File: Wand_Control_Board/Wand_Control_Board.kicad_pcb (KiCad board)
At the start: 2 copper layers, 11.5 x 40.1 mm, 6 parts, among them J1 Conn_01x03_Socket, J2 Conn_01x03_Socket, J3 Conn_01x03_Socket, J5 Conn_01x05_Socket, J8 Conn_01x02_Socket, U1 ATtiny85-20P

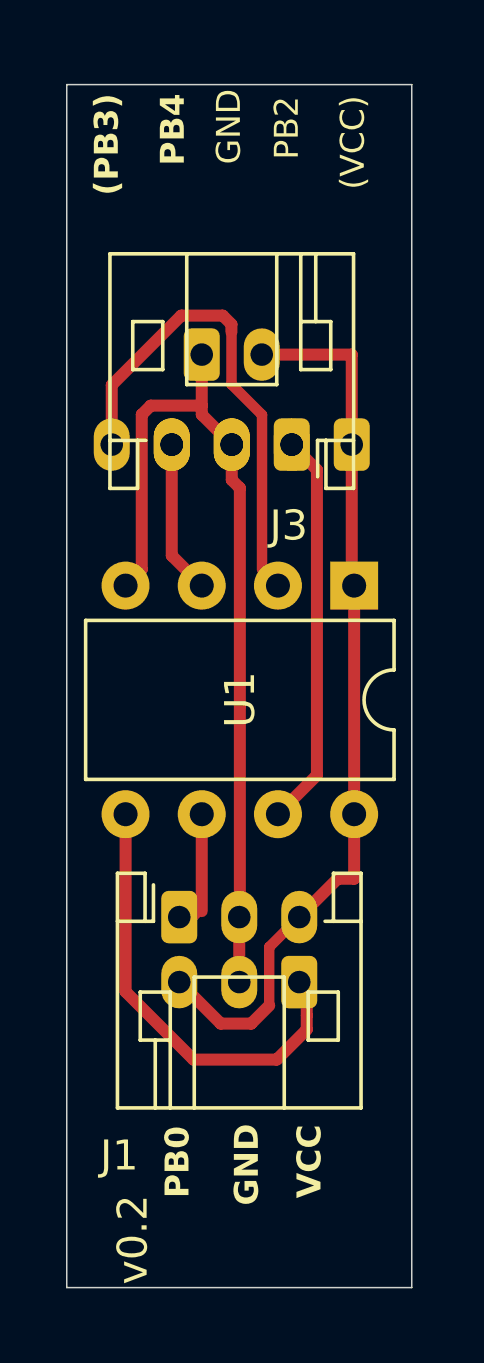
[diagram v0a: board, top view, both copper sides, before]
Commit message: added unneeded prog pad
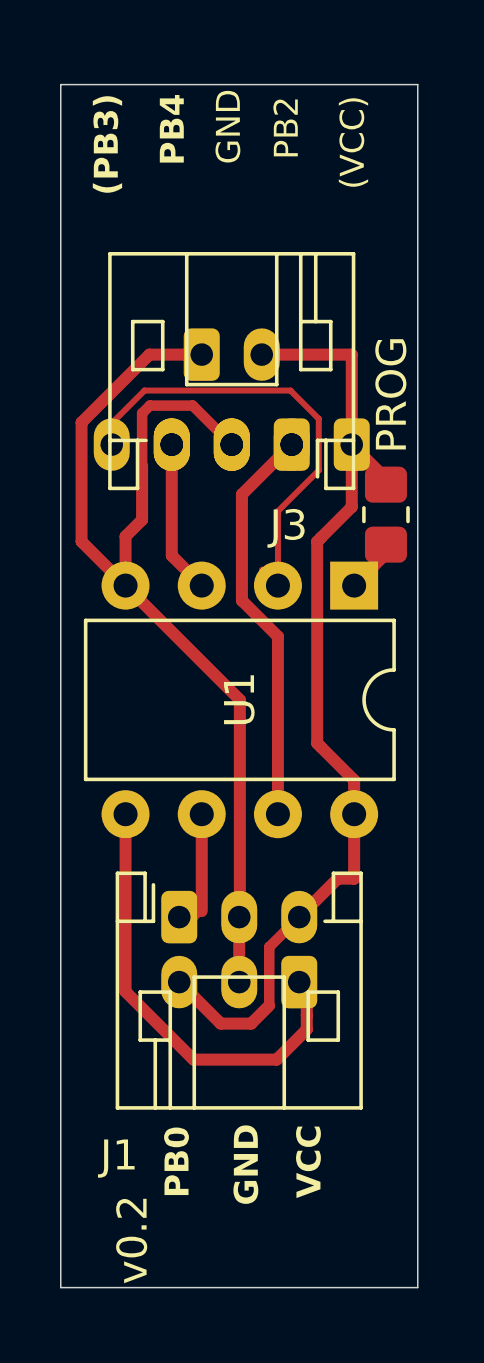
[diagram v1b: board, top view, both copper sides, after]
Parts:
- added PROG: 0, Resistor_SMD:R_0805_2012Metric_Pad1.20x1.40mm_HandSolder, F.Cu at (155.6, 54.8)
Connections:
- J5 pad 2: Net-(J3-Pin_1) -> Net-(J3-Pin_3)
- J5 pad 4: Net-(J3-Pin_3) -> Net-(J3-Pin_1)
- U1 pad 1: VCC -> Net-(U1-~{RESET}/PB5)
- U1 pad 3: Net-(J3-Pin_1) -> Net-(J3-Pin_3)
- U1 pad 7: Net-(J3-Pin_3) -> Net-(J3-Pin_1)
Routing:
- net Net-(J3-Pin_1): track 5.11 -> 13.5 mm
- net Net-(J3-Pin_3): track 13.2 -> 5.11 mm
- net GND: track 29.9 -> 35.8 mm
- net VCC: track 30.0 -> 33.0 mm
- net Net-(J5-Pin_5): track 16.4 -> 14.6 mm
- net Net-(U1-~{RESET}/PB5): track 0.00 -> 1.74 mm
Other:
- board size 11.5 x 40.1 mm -> 11.9 x 40.1 mm

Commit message: removed unneeded progam pad
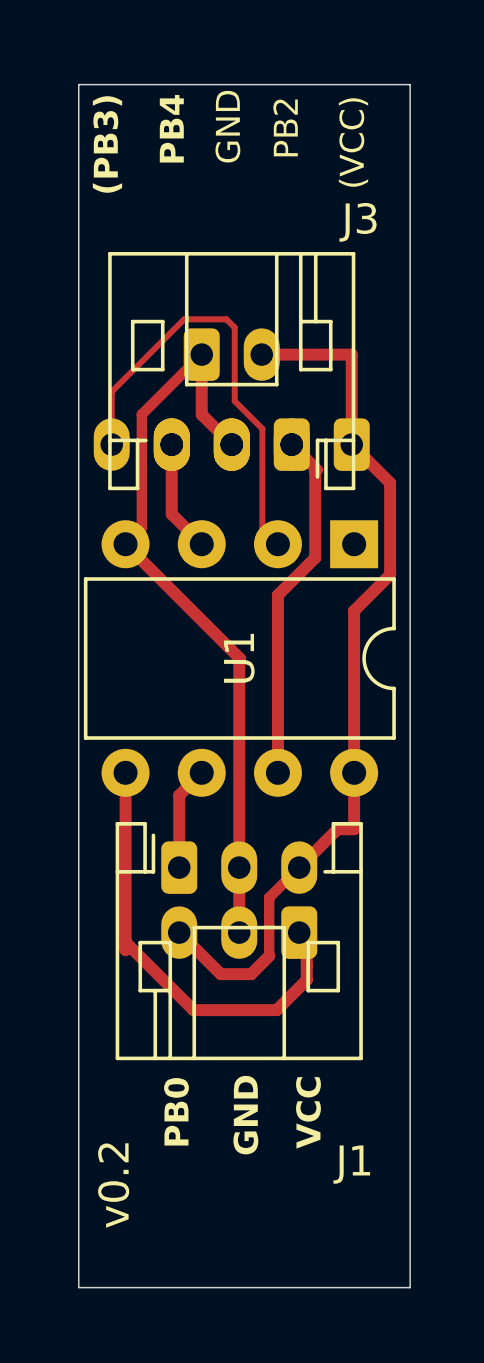
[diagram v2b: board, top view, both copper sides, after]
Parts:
- removed PROG: 0, Resistor_SMD:R_0805_2012Metric_Pad1.20x1.40mm_HandSolder
- moved J1 1.65 mm to (148.8, 66.6)
- moved J2 1.65 mm to (152.8, 68.8)
- moved U1 1.38 mm to (154.6, 55.8)
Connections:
- J5 pad 4: Net-(J3-Pin_1) -> Net-(J3-Pin_3)
- U1 pad 1: Net-(U1-~{RESET}/PB5) -> unconnected-(U1-~{RESET}/PB5-Pad1)
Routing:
- net GND: track 35.8 -> 26.3 mm
- net VCC: track 33.0 -> 29.4 mm
- net Net-(J3-Pin_1): track 13.5 -> 11.7 mm
- net Net-(U1-~{RESET}/PB5): track 1.74 -> 0.00 mm
- net Net-(J3-Pin_3): track 5.11 -> 3.73 mm
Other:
- board size 11.9 x 40.1 mm -> 11 x 40.1 mm

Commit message: outputs and cleaner silkscreen
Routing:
- net Net-(J5-Pin_5): track 14.8 -> 15.9 mm
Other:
- board size 11 x 40.1 mm -> 11 x 38.3 mm

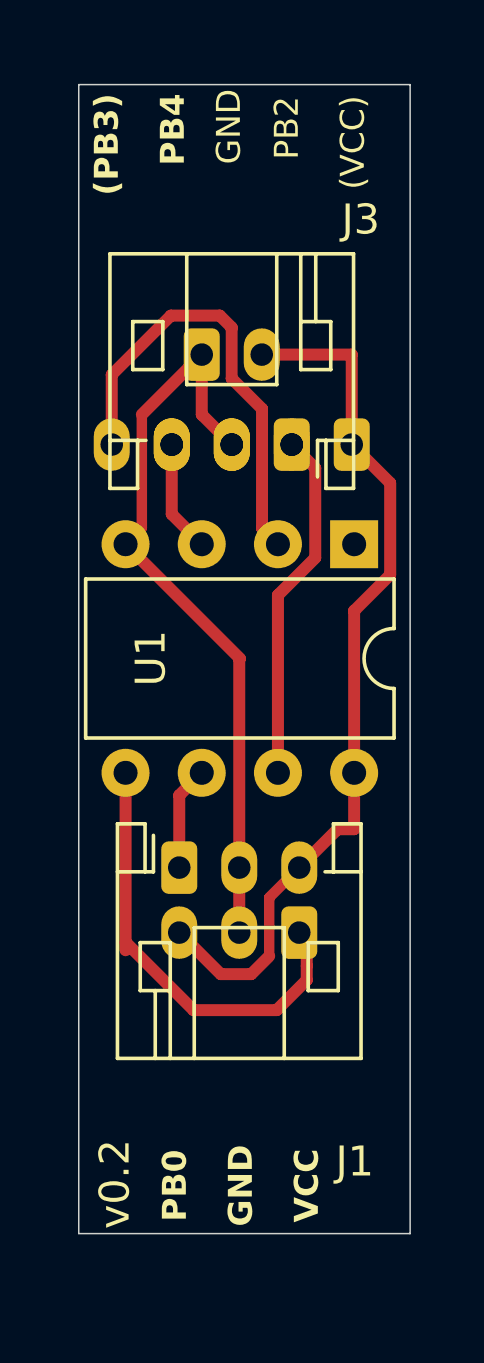
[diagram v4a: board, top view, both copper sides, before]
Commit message: flipped parts to make solder easier
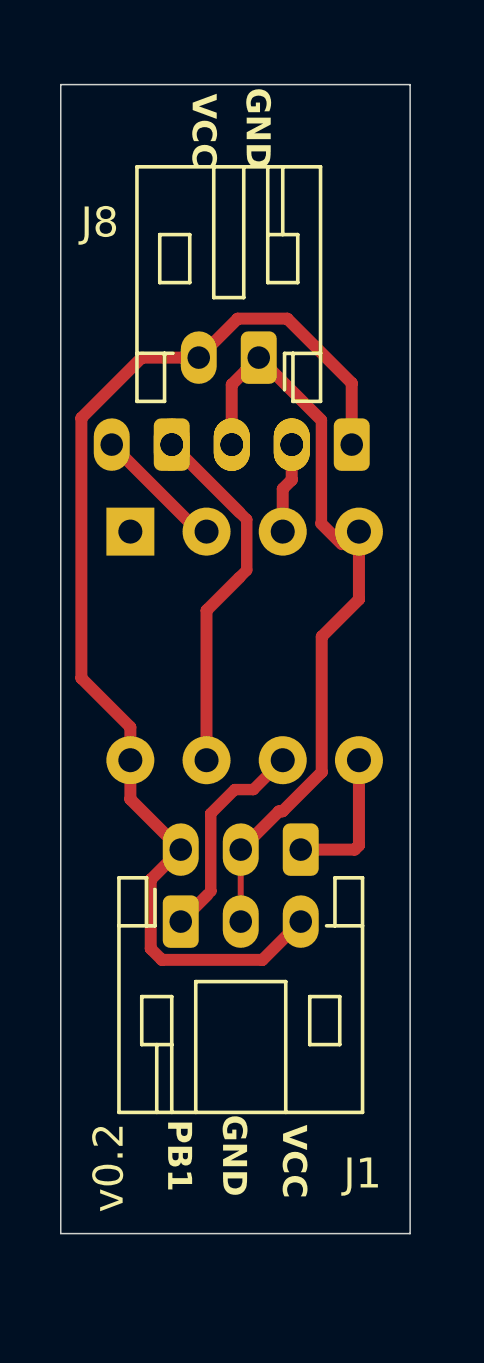
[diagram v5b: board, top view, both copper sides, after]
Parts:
- J3, U1: moved to B.Cu
- J8: moved to F.Cu
- moved U1 7.47 mm to (147.1, 55.4)
- moved J3 4.00 mm to (148.5, 52.5), turned to 0 degrees
- moved J2 2.77 mm to (152.8, 66.0)
- moved J8 1.90 mm to (151.4, 49.6), turned to 180 degrees
- moved J1 1.80 mm to (148.8, 68.4)
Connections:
- J5 pad 4: Net-(J3-Pin_3) -> Net-(J3-Pin_1)
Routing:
- net Net-(J5-Pin_5): track 15.9 -> 4.36 mm
- net Net-(J2-Pin_1): track 14.3 -> 4.84 mm
- net VCC: track 29.4 -> 38.5 mm
- net Net-(J1-Pin_1): track 3.47 -> 7.16 mm
- net Net-(J3-Pin_1): track 11.8 -> 12.3 mm
- net Net-(J3-Pin_3): track 3.73 -> 4.25 mm
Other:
- board size 11 x 38.3 mm -> 11.6 x 38.3 mm
